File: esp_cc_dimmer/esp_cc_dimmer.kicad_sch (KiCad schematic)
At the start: 0 parts

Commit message: update:wq
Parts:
- added C1, C2: 1uF, Capacitor_SMD:C_0603_1608Metric, symbol Device:C
- added C10, C8, C9: 10u, Capacitor_SMD:C_0805_2012Metric, symbol Device:C
- added C3: 1u, Capacitor_SMD:C_0603_1608Metric, symbol Device:C
- added J1, J2: Conn_01x02, symbol Connector_Generic:Conn_01x02
- added PS1: NLDD-1050H, footprints:NLDD1050H, symbol NLDD-1050H:NLDD-1050H
- added R1, R2: 4.7k, Resistor_SMD:R_0603_1608Metric, symbol Device:R
- added SW1: RotaryEncoder_Switch, Rotary_Encoder:RotaryEncoder_Alps_EC11E-Switch_Vertical_H20mm_MountingHoles, symbol Device:RotaryEncoder_Switch
- added U1: ESP32-C3-SuperMini, footprints:ESP32-C3-SuperMini, symbol ESP32-C3-SuperMini:ESP32-C3-SuperMini
- added U2: VEML7700-TR, footprints:VEML7700-TR, symbol VEML7700_TR:VEML7700-TR
- added U4: (no value), LX8015:LX8015, symbol LX8015:LX8015
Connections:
- new net: SW1.A, U1.2 (GPIO1)
- new net: SW1.B, U1.1 (GPIO0)
- new net: SW1.S1, U1.4 (GPIO3)
- new net: C10.2, C9.1
- new net: C3.2, U2.3 (GND)
- new net +3V3: C2.1, C3.1, R1.1, R2.1, U1.6 (3V3), U2.2 (VDD)
- new net +48V: C10.1, J2.1 (Pin_1), PS1.23 (+VIN_1), PS1.24 (+VIN_2), U4.1 (Vin)
- new net +5V: C1.1, C8.1, U1.8 (5V), U4.4 (Vout)
- new net GND: C1.2, C2.2, C8.2, C9.2, J2.2 (Pin_2), PS1.1 (-VIN_1), PS1.2 (-VIN_2), SW1.C, SW1.S2, U1.7 (GND), U4.2 (GND), U4.3 (GND)
- new net LED_PWM: PS1.22 (PWM_DIM), U1.14 (GPIO10)
- new net SCL: R1.2, U1.13 (GPIO9), U2.1 (SCL)
- new net SDA: R2.2, U1.12 (GPIO8), U2.4 (SDA)
- new net Vled+: J1.1 (Pin_1), PS1.13 (+VOUT_1), PS1.14 (+VOUT_2)
- new net Vled-: J1.2 (Pin_2), PS1.11 (-VOUT_1), PS1.12 (-VOUT_2)
- no-connect marks 0 -> 7
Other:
- note added: "Any of NLDD 350~1050H will work"

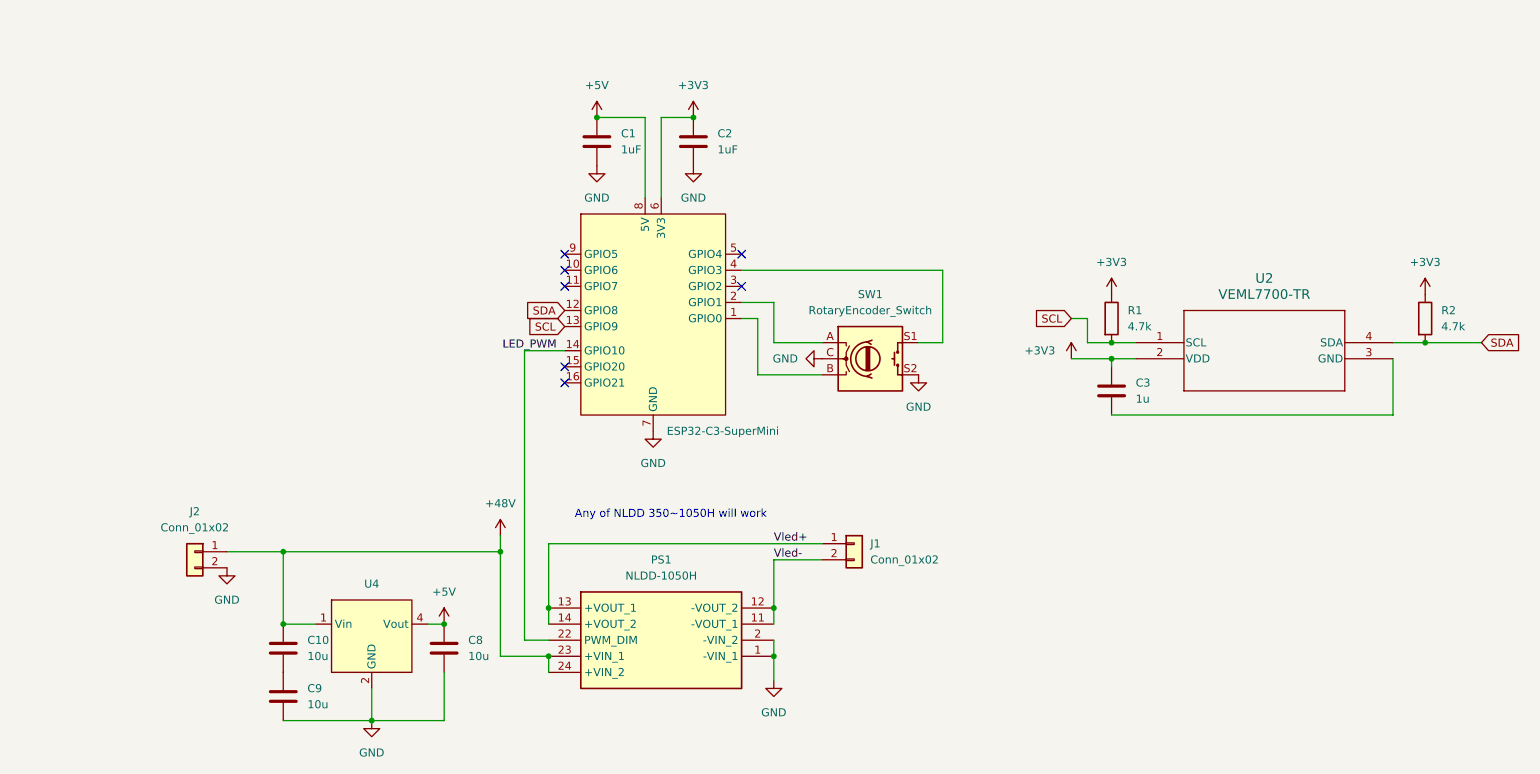
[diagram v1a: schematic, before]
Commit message: wip: cc driver
need to double check esp32 pinout
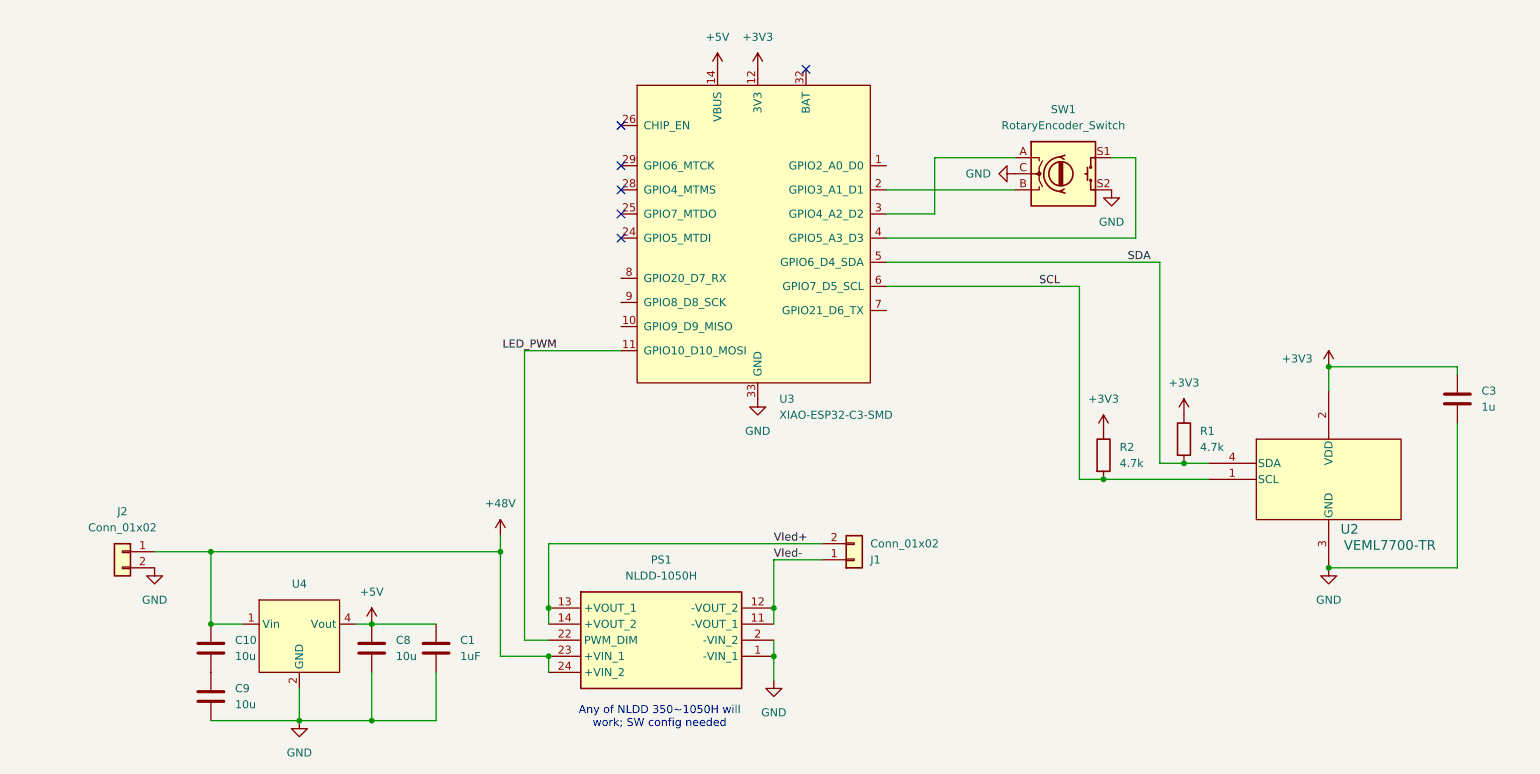
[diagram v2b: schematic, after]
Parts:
- removed C2: 1uF, Capacitor_SMD:C_0603_1608Metric, symbol Device:C
- removed U1: ESP32-C3-SuperMini, footprints:ESP32-C3-SuperMini, symbol ESP32-C3-SuperMini:ESP32-C3-SuperMini
- added U3: XIAO-ESP32-C3-SMD, footprints:XIAO-ESP32-C3-DIP-SMD, symbol Seeed_Studio_XIAO_Series:XIAO-ESP32-C3-SMD
- J1, J2: footprint (none) -> Connector_Phoenix_MC:PhoenixContact_MC_1,5_2-G-3.81_1x02_P3.81mm_Horizontal
- U2: footprint footprints:VEML7700-TR -> VEML7700-TR
- U4: footprint LX8015:LX8015 -> footprints:LX8015
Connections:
- net +3V3: now also U3.12 (3V3)
- net +5V: now also U3.14 (VBUS)
- net GND: now also C3.2, U2.3 (GND), U3.13 (GND), U3.27 (GND), U3.33 (GND)
- net LED_PWM: now also U3.11 (GPIO10_D10_MOSI)
- net SCL: now also R2.2, U3.6 (GPIO7_D5_SCL); no longer R1.2
- net SDA: now also R1.2, U3.5 (GPIO6_D4_SDA); no longer R2.2
- net Vled+: now also J1.2 (Pin_2); no longer J1.1 (Pin_1)
- net Vled-: now also J1.1 (Pin_1); no longer J1.2 (Pin_2)
- net at SW1.A: now also U3.3 (GPIO4_A2_D2)
- net at SW1.B: now also U3.2 (GPIO3_A1_D1)
- net at SW1.S1: now also U3.4 (GPIO5_A3_D3)
- no-connect marks 7 -> 6
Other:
- note added: "Any of NLDD 350~1050H will work; SW config needed"
- note removed: "Any of NLDD 350~1050H will work"
- moved on the sheet: C1, C10, C3, C8, C9, J2, R1, R2, SW1, U4

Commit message: done maybe
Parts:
- SW1: symbol Device:RotaryEncoder_Switch -> Device:RotaryEncoder_Switch_MP
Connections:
- net GND: now also SW1.MP
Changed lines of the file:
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@@
+		(color 0 0 0 0)
+	)
+	(junction
+		(at 198.12 55.88)
+		(diameter 0)
 		(color 0 0 0 0)
 	)
@@
 	(wire
 		(pts
+			(xy 187.96 58.42) (xy 187.96 59.69)
+		)
+		(stroke
+			(width 0)
+			(type default)
+		)
+	)
+	(wire
+		(pts
 			(xy 213.36 62.23) (xy 213.36 93.98)
 		)
@@
 	(wire
 		(pts
-			(xy 209.55 58.42) (xy 170.18 58.42)
+			(xy 170.18 58.42) (xy 187.96 58.42)
 		)
 		(stroke
@@
 	(wire
 		(pts
+			(xy 187.96 59.69) (xy 209.55 59.69)
+		)
+		(stroke
+			(width 0)
+			(type default)
+		)
+	)
+	(wire
+		(pts
 			(xy 88.9 127) (xy 88.9 134.62)
 		)
@@
 	(wire
 		(pts
+			(xy 205.74 55.88) (xy 205.74 50.8)
+		)
+		(stroke
+			(width 0)
+			(type default)
+		)
+	)
+	(wire
+		(pts
 			(xy 200.66 66.04) (xy 200.66 96.52)
 		)
@@
 	(wire
 		(pts
-			(xy 209.55 45.72) (xy 209.55 58.42)
+			(xy 209.55 45.72) (xy 209.55 59.69)
 		)
 		(stroke
@@
 		(pts
 			(xy 217.17 93.98) (xy 220.98 93.98)
+		)
+		(stroke
+			(width 0)
+			(type default)
+		)
+	)
+	(wire
+		(pts
+			(xy 198.12 55.88) (xy 205.74 55.88)
 		)
 		(stroke
@@
 	)
 	(symbol
-		(lib_id "Device:RotaryEncoder_Switch")
+		(lib_id "Device:RotaryEncoder_Switch_MP")
 		(at 198.12 48.26 0)
 		(unit 1)
@@
 		)
 		(property "Datasheet" ""
-			(at 198.12 41.656 0)
-			(hide yes)
-			(show_name no)
-			(do_not_autoplace no)
-			(effects
-				(font
-					(size 1.27 1.27)
-				)
-			)
-		)
-		(property "Description" "Rotary encoder, dual channel, incremental quadrate outputs, with switch"
-			(at 198.12 48.26 0)
+			(at 198.12 60.96 0)
+			(hide yes)
+			(show_name no)
+			(do_not_autoplace no)
+			(effects
+				(font
+					(size 1.27 1.27)
+				)
+			)
+		)
+		(property "Description" "Rotary encoder, dual channel, incremental quadrate outputs, with switch and MP Pin"
+			(at 198.12 63.5 0)
 			(hide yes)
 			(show_name no)
@@
 		)
 		(pin "S1"
+		)
+		(pin "MP"
 		)
 		(instances
@@
 	(symbol
 		(lib_id "power:GND")
-		(at 205.74 50.8 0)
+		(at 198.12 55.88 0)
 		(unit 1)
 		(body_style 1)
@@
 		(in_pos_files yes)
 		(dnp no)
-		(fields_autoplaced yes)
 		(property "Reference" "#PWR012"
-			(at 205.74 57.15 0)
+			(at 198.12 62.23 0)
 			(hide yes)
 			(show_name no)
@@
 		)
 		(property "Value" "GND"
-			(at 205.74 55.88 0)
+			(at 194.31 57.658 0)
 			(show_name no)
 			(do_not_autoplace no)
@@
 		)
 		(property "Footprint" ""
-			(at 205.74 50.8 0)
+			(at 198.12 55.88 0)
 			(hide yes)
 			(show_name no)
@@
 		)
 		(property "Datasheet" ""
-			(at 205.74 50.8 0)
+			(at 198.12 55.88 0)
 			(hide yes)
 			(show_name no)
@@
 		)
 		(property "Description" "Power symbol creates a global label with name \"GND\" , ground"
-			(at 205.74 50.8 0)
-			(hide yes)
-			(show_name no)
+			(at 198.12 55.88 0)
+			(hide yes)
+			(show_name no)

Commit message: update
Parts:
- removed C10, C9: 10u, Capacitor_SMD:C_0805_2012Metric, symbol Device:C
- added C11: 4.7u 100V, Capacitor_SMD:C_1210_3225Metric_Pad1.33x2.70mm_HandSolder, symbol Device:C
- added C2: 100u 63V, Capacitor_THT:CP_Radial_D8.0mm_P3.50mm, symbol Device:C_Polarized
- added H1, H2: MountingHole, MountingHole:MountingHole_3.2mm_M3, symbol Mechanical:MountingHole
- J1, J2: value Conn_01x02 -> WJ15EDGRC-3.81-02P-14-00A; LCSC (none) -> C8387
- SW1: value RotaryEncoder_Switch -> EC11E15244G1; LCSC (none) -> C370970
- U2: footprint VEML7700-TR -> footprints:VEML7700-TR
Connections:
- net +48V: now also C11.1, C2.1
- net GND: now also C11.2, C2.2

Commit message: fix bugs, add esphome config
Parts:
- C3: value 1u -> 1uF
- C8: footprint Capacitor_SMD:C_0805_2012Metric -> Capacitor_SMD:C_1210_3225Metric_Pad1.33x2.70mm_HandSolder
- U4: value (none) -> LX8015
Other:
- moved on the sheet: C8
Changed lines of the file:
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@@
 	)
 	(junction
-		(at 88.9 134.62)
-		(diameter 0)
-		(color 0 0 0 0)
-	)
-	(junction
 		(at 63.5 134.62)
 		(diameter 0)
@@
 		(color 0 0 0 0)
 	)
+	(junction
+		(at 88.9 134.62)
+		(diameter 0)
+		(color 0 0 0 0)
+	)
 	(no_connect
 		(at 157.48 31.75)
@@
 	(wire
 		(pts
-			(xy 88.9 127) (xy 88.9 134.62)
+			(xy 88.9 132.08) (xy 88.9 134.62)
 		)
 		(stroke
@@
 	(wire
 		(pts
+			(xy 88.9 124.46) (xy 88.9 119.38)
+		)
+		(stroke
+			(width 0)
+			(type default)
+		)
+	)
+	(wire
+		(pts
 			(xy 99.06 134.62) (xy 88.9 134.62)
 		)
@@
 			)
 		)
-		(property "Value" ""
+		(property "Value" "LX8015"
 			(at 77.47 119.38 0)
 			(show_name no)
@@
 			)
 		)
-		(property "Value" "1u"
+		(property "Value" "1uF"
 			(at 264.16 85.0899 0)
 			(show_name no)
@@
 	(symbol
 		(lib_id "Device:C")
-		(at 88.9 123.19 0)
+		(at 88.9 128.27 0)
 		(unit 1)
 		(body_style 1)
@@
 		(fields_autoplaced yes)
 		(property "Reference" "C8"
-			(at 92.71 121.9199 0)
+			(at 92.71 126.9999 0)
 			(show_name no)
 			(do_not_autoplace no)
@@
 		)
 		(property "Value" "10u"
-			(at 92.71 124.4599 0)
+			(at 92.71 129.5399 0)
 			(show_name no)
 			(do_not_autoplace no)
@@
 			)
 		)
-		(property "Footprint" "Capacitor_SMD:C_0805_2012Metric"
-			(at 89.8652 127 0)
+		(property "Footprint" "Capacitor_SMD:C_1210_3225Metric_Pad1.33x2.70mm_HandSolder"
+			(at 89.8652 132.08 0)
 			(hide yes)
 			(show_name no)
@@
 		)
 		(property "Datasheet" ""
-			(at 88.9 123.19 0)
+			(at 88.9 128.27 0)
 			(hide yes)
 			(show_name no)
@@
 		)
 		(property "Description" "Unpolarized capacitor"
-			(at 88.9 123.19 0)
+			(at 88.9 128.27 0)
 			(hide yes)
 			(show_name no)
